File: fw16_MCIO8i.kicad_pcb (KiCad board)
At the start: 4 copper layers, 118.7 x 72.5 mm, 24 parts

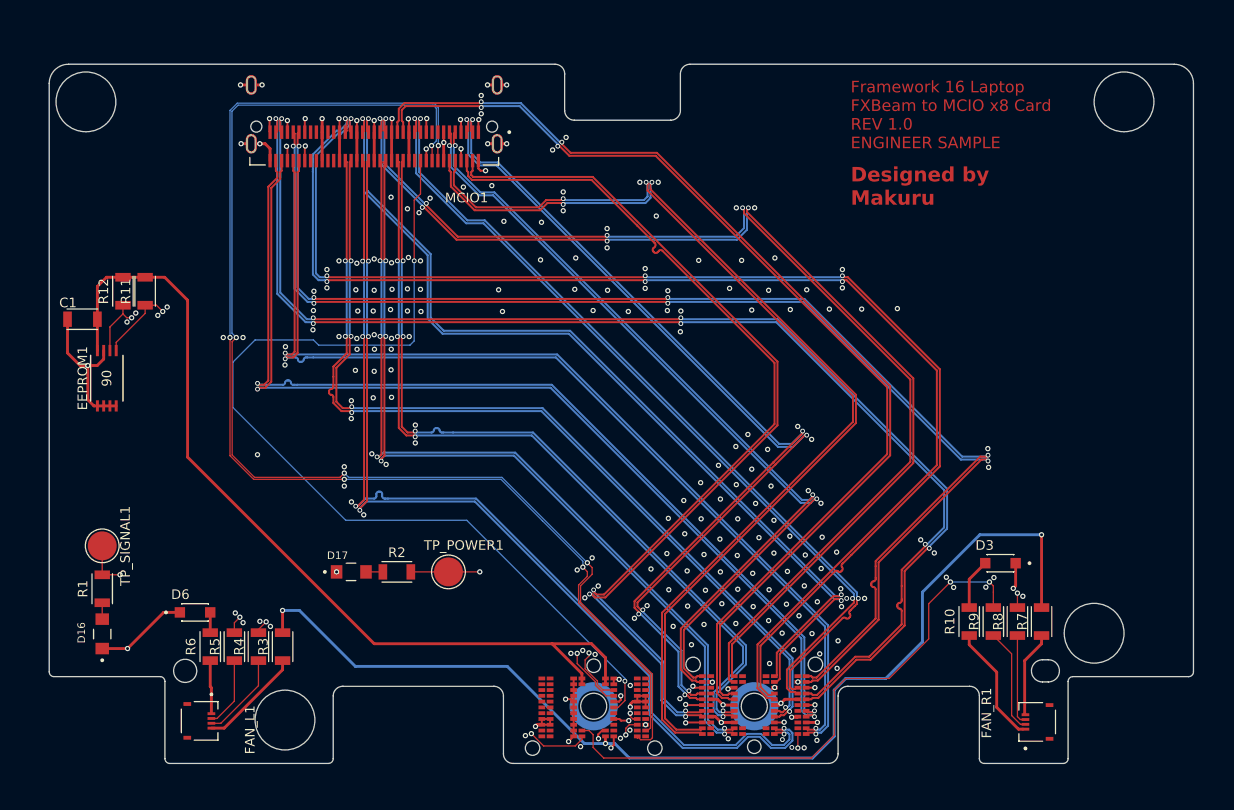
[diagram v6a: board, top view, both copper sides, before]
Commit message: Fixed skew and silkscreen
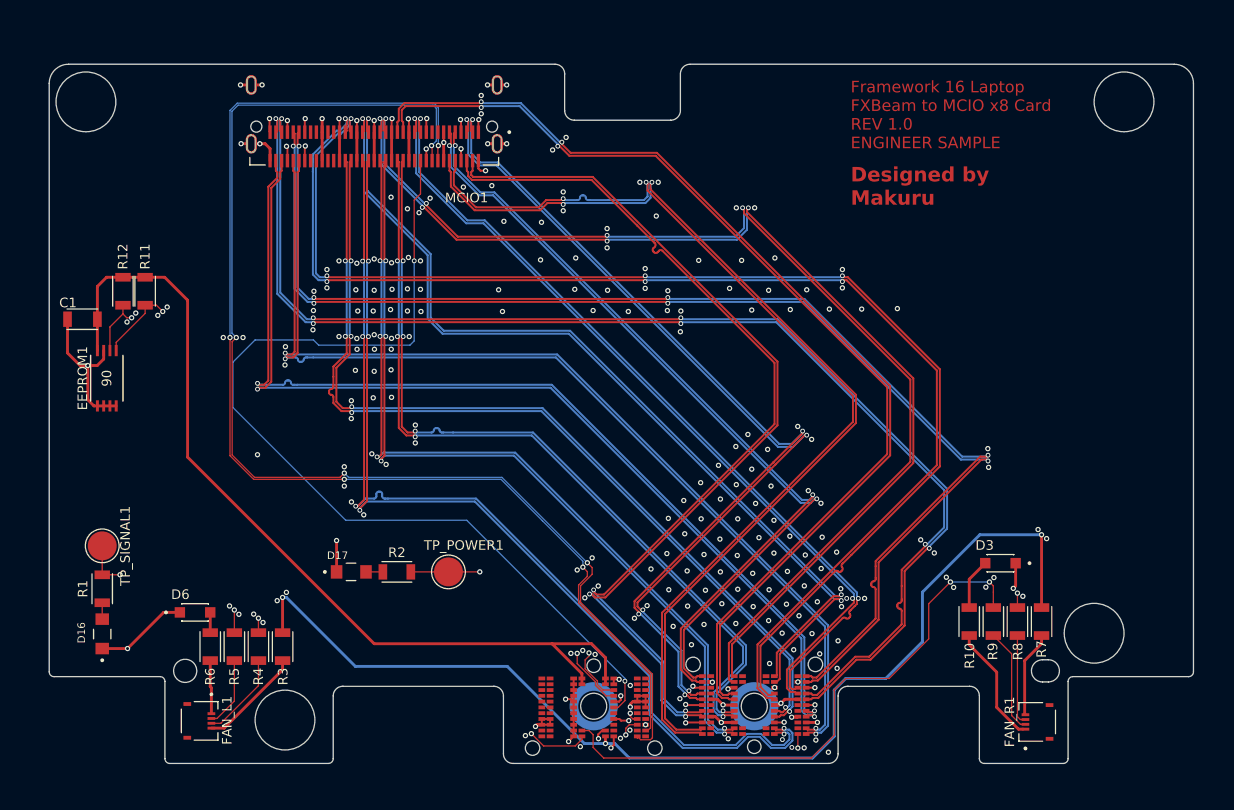
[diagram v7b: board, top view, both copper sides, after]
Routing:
- net GND: track 123.7 -> 126.9 mm, vias 251 -> 256
- net 12V_FAN: track 111.1 -> 113.0 mm
- net /FAN0_PWM: track 44.9 -> 46.3 mm
- net /FAN0_SPD: track 45.2 -> 46.2 mm
- net /TX1+: track 103.4 -> 103.9 mm

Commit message: MPN & LCSC
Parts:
- C1: footprint capacitor:C_Wurth_WCAP-CSGP-1206_H0.8 -> capacitor:C_Wurth_WCAP-CSGP-1206_H1.6
